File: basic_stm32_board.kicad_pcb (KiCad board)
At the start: 4 copper layers, 2 x 7.5 mm, 61 parts, among them J1 Screw_Terminal_01x02, J2 USB_B_Micro, J3 Conn_01x04, J4 Conn_01x04, J5 Conn_ARM_JTAG_SWD_10, Q1 AO3401A, SW1 SW_SPDT, U1 STM32F405RGT6, U2 MP2303ADN, U3 USBLC6-2SC6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

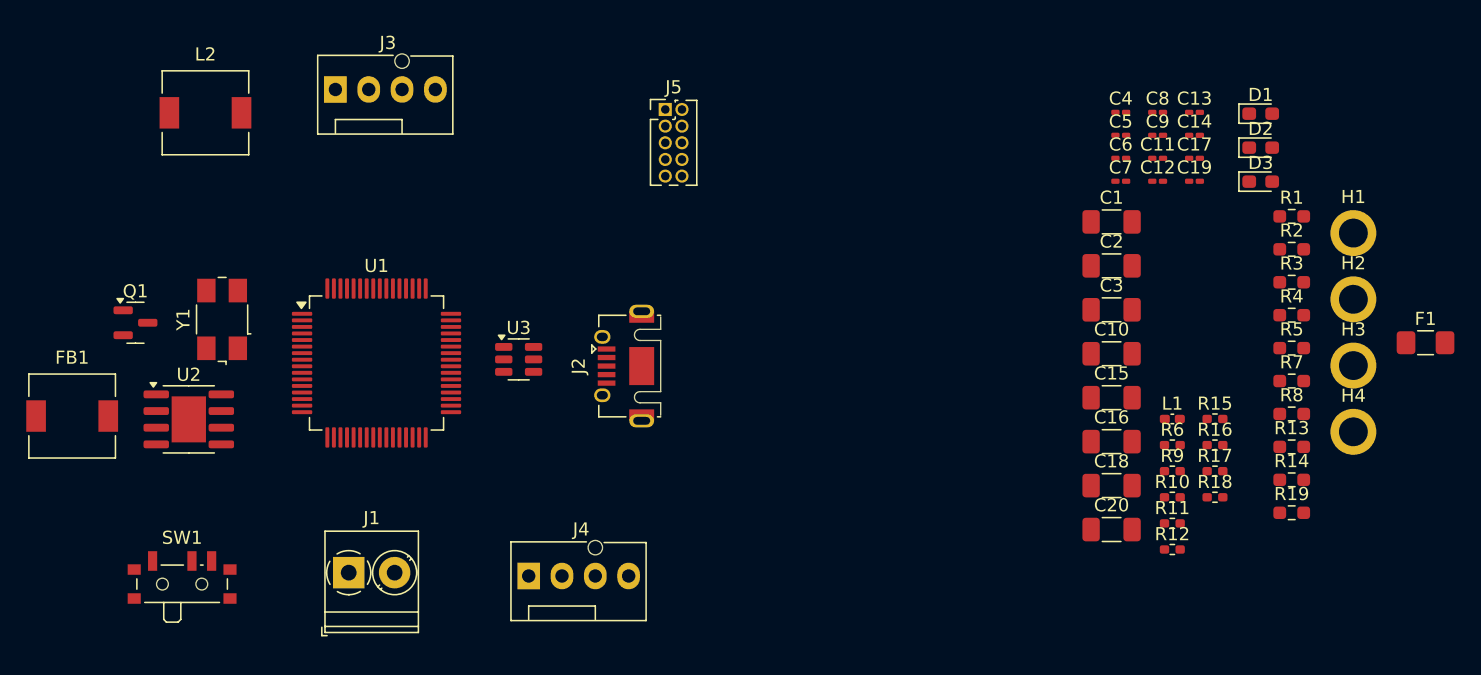
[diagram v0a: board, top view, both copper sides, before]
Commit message: removed all DRC errors
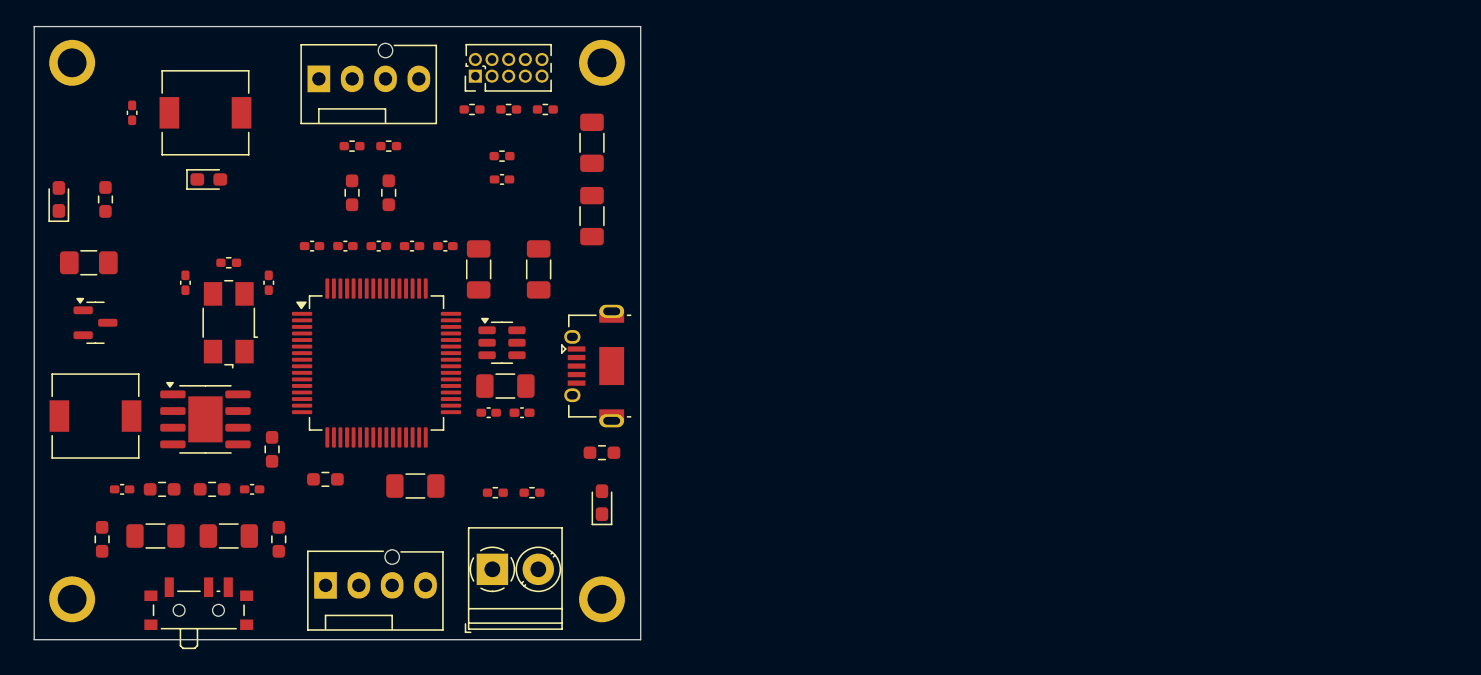
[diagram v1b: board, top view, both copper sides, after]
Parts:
- C11, C12, C13, C14, C17, C19, C4, C5, C6, C7, C8, C9: footprint Capacitor_SMD:C_0201_0603Metric_Pad0.64x0.40mm_HandSolder -> Capacitor_SMD:C_0402_1005Metric_Pad0.74x0.62mm_HandSolder
- moved F1 102.1 mm to (134.9, 89.2)
- moved H2 99.3 mm to (133.6, 73.9)
- moved H4 98.5 mm to (133.6, 114.8)
- moved R19 93.5 mm to (136.1, 84.3), turned to 90 degrees
- moved D3 91.6 mm to (132.6, 84.3), turned to 90 degrees
- moved R8 91.2 mm to (135.9, 110.2), turned to 90 degrees
- moved R4 87.1 mm to (140.5, 106.4)
- moved C13 86.6 mm to (137.4, 106.4)
- moved R5 83.0 mm to (144.3, 106.4)
- moved C17 81.1 mm to (138.2, 77.7), turned to 90 degrees
- moved D1 80.3 mm to (144.0, 82.8)
- moved R2 80.3 mm to (149.4, 110.2), turned to 90 degrees
- moved R14 77.8 mm to (148.8, 103.4), turned to 90 degrees
- moved C14 76.7 mm to (147.3, 106.4)
- moved C9 75.0 mm to (142.2, 90.7), turned to 90 degrees
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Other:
- board size 2 x 7.5 mm -> 46.2 x 46.7 mm

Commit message: some layout adjustement
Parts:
- moved J1 39.5 mm to (136.1, 86.4), turned to -90 degrees
- moved C15 12.7 mm to (152.7, 110.5), turned to -90 degrees
- moved C16 11.2 mm to (156.7, 110.5), turned to -90 degrees
- moved F1 9.88 mm to (144.3, 86.1)
- moved J4 7.82 mm to (160.5, 112.0)
- moved Q1 4.85 mm to (140.2, 94.2)
- moved L1 3.64 mm to (168.7, 104.1)
- moved C12 3.59 mm to (165.9, 104.1)
- moved R8 3.53 mm to (137.7, 113.3), turned to -90 degrees
- moved R2 3.34 mm to (148.8, 113.5)
- moved D3 2.54 mm to (132.6, 81.8)
- moved R19 2.54 mm to (136.1, 81.8)
- moved H3 1.78 mm to (174.0, 113.0)
- moved H4 1.78 mm to (133.6, 113.0)
- moved SW1 1.78 mm to (143.3, 113.5)
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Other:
- board size 46.2 x 46.7 mm -> 46.2 x 44.7 mm

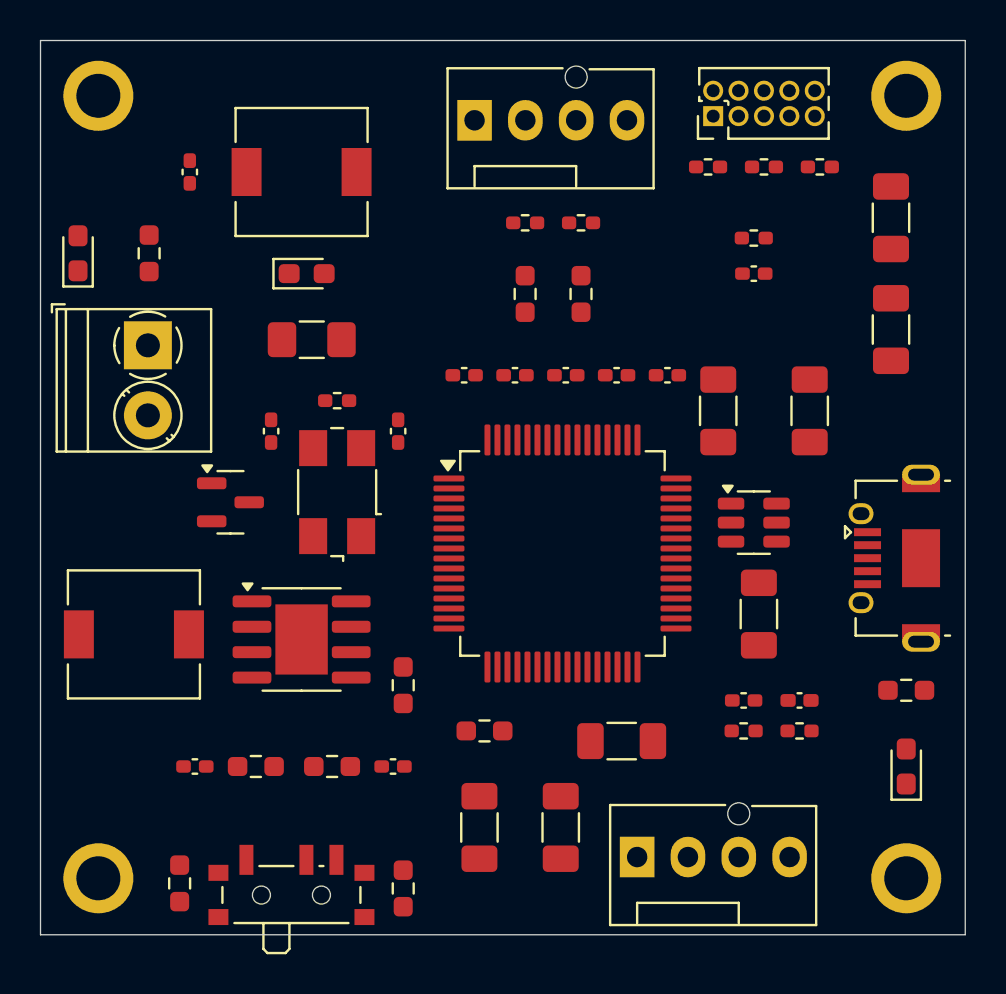
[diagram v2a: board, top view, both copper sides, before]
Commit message: Working now on signal traces..
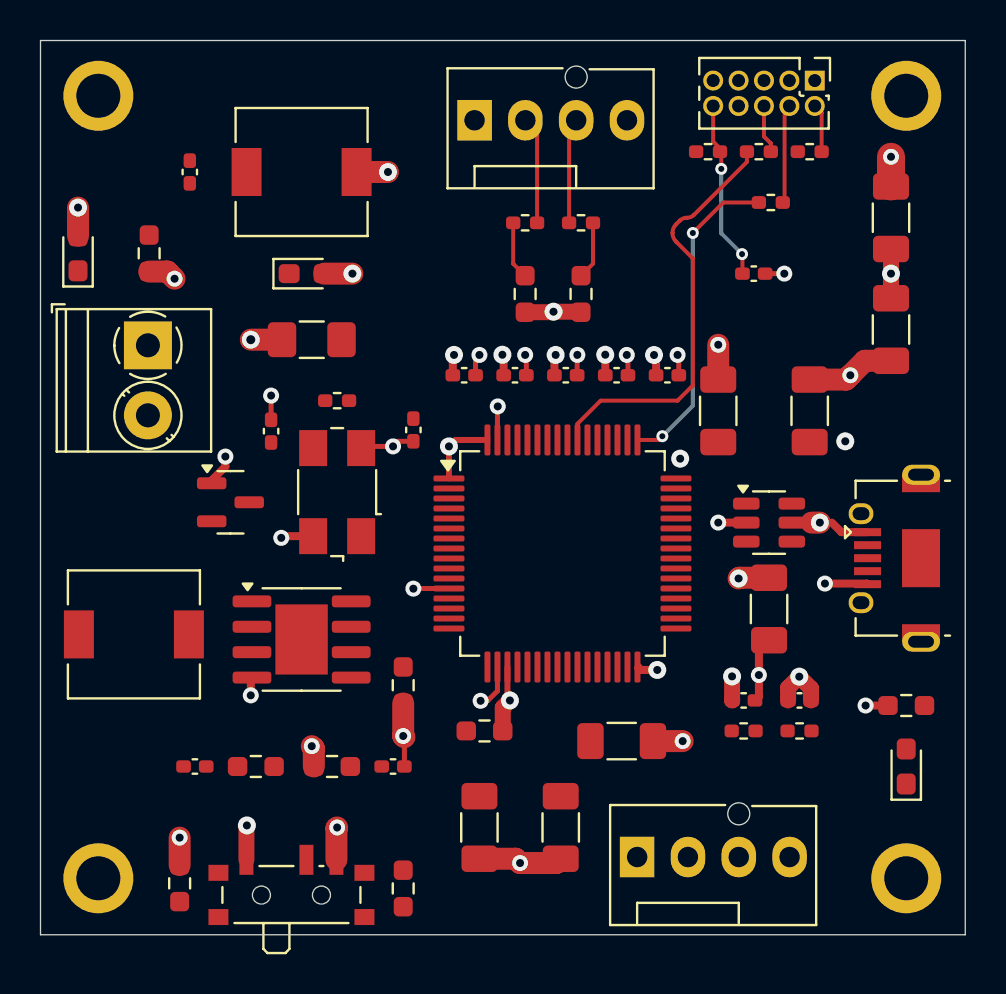
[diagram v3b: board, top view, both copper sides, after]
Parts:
- moved J5 5.38 mm to (169.4, 73.2), turned to -90 degrees
- moved R18 4.89 mm to (164.1, 76.7)
- moved R15 3.61 mm to (167.2, 79.2)
- moved R17 3.14 mm to (166.6, 76.7)
- moved R16 2.41 mm to (169.2, 76.7)
- moved C11 0.76 mm to (149.4, 90.6), turned to -90 degrees
- moved R1 0.76 mm to (174.0, 104.4), turned to 180 degrees
- moved U3 0.76 mm to (167.1, 95.2)
- moved C10 0.57 mm to (167.1, 99.6)
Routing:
- net GND: track 0.00 -> 50.2 mm, vias 0 -> 28
- net +3.3VA: track 0.00 -> 33.6 mm, vias 0 -> 20
- net SWO: track 0.00 -> 21.2 mm
- net SWCLK: track 0.00 -> 16.0 mm, vias 0 -> 2
- net Net-(J5-~{RESET}): track 0.00 -> 8.99 mm, vias 0 -> 2
- net Net-(J3-Pin_2): track 0.00 -> 5.37 mm
- net Net-(J3-Pin_3): track 0.00 -> 5.27 mm
- net Net-(J5-SWCLK/TCK): track 0.00 -> 4.96 mm
- net I2C1_SDA: track 0.00 -> 2.89 mm
- net I2C1_SCL: track 0.00 -> 2.89 mm
- net Net-(J5-SWO/TDO): track 0.00 -> 2.43 mm
- net Net-(J5-SWDIO/TMS): track 0.00 -> 2.43 mm
- net P,+12: track 0.00 -> 1.56 mm, vias 0 -> 1
- added copper zone on In2.Cu, net +3.3VA
- added copper zone on In1.Cu, net GND
- added copper zone on In2.Cu, net P,+12

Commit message: experimenting with tarces placement..
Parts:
- moved D1 14.9 mm to (134.8, 94.5), turned to 180 degrees
- moved R6 5.36 mm to (148.6, 93.6), turned to 90 degrees
- moved R2 3.82 mm to (149.1, 109.7), turned to 180 degrees
- moved C1 0.57 mm to (160.0, 106.7)
- turned R4 to 90 degrees
- turned R5 to -90 degrees
- turned U3 to 180 degrees
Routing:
- net Buck_IN: track 0.00 -> 45.0 mm, vias 0 -> 2
- net Net-(U2-SW): track 0.00 -> 34.0 mm, vias 0 -> 2
- net LED_STATUS: track 0.00 -> 30.6 mm, vias 0 -> 2
- net NRST: track 0.00 -> 26.6 mm, vias 0 -> 2
- net Net-(U2-BS): track 0.00 -> 25.2 mm, vias 0 -> 2
- net SWDIO: track 0.00 -> 21.3 mm
- net BOOT0: track 0.00 -> 20.8 mm, vias 0 -> 2
- net Buck_COMP: track 0.00 -> 15.4 mm, vias 0 -> 2
- net USART3_RX: track 0.00 -> 15.4 mm, vias 0 -> 2
- net Buck_EN: track 0.00 -> 15.3 mm, vias 0 -> 2
- net unconnected-(J2-Shield-Pad6)_2: track 0.00 -> 14.0 mm
- net USART3_TX: track 0.00 -> 12.3 mm, vias 0 -> 2
- net HSE_IN: track 0.00 -> 12.2 mm
- net +3.3VA: track 33.6 -> 45.5 mm
- net Buck_SS: track 0.00 -> 11.6 mm, vias 0 -> 2
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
